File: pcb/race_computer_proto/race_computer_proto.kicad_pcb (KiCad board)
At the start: 4 copper layers, 200.7 x 125.7 mm, 17 parts, among them U1 Teensy4.0, U3 SN74LVC245APW

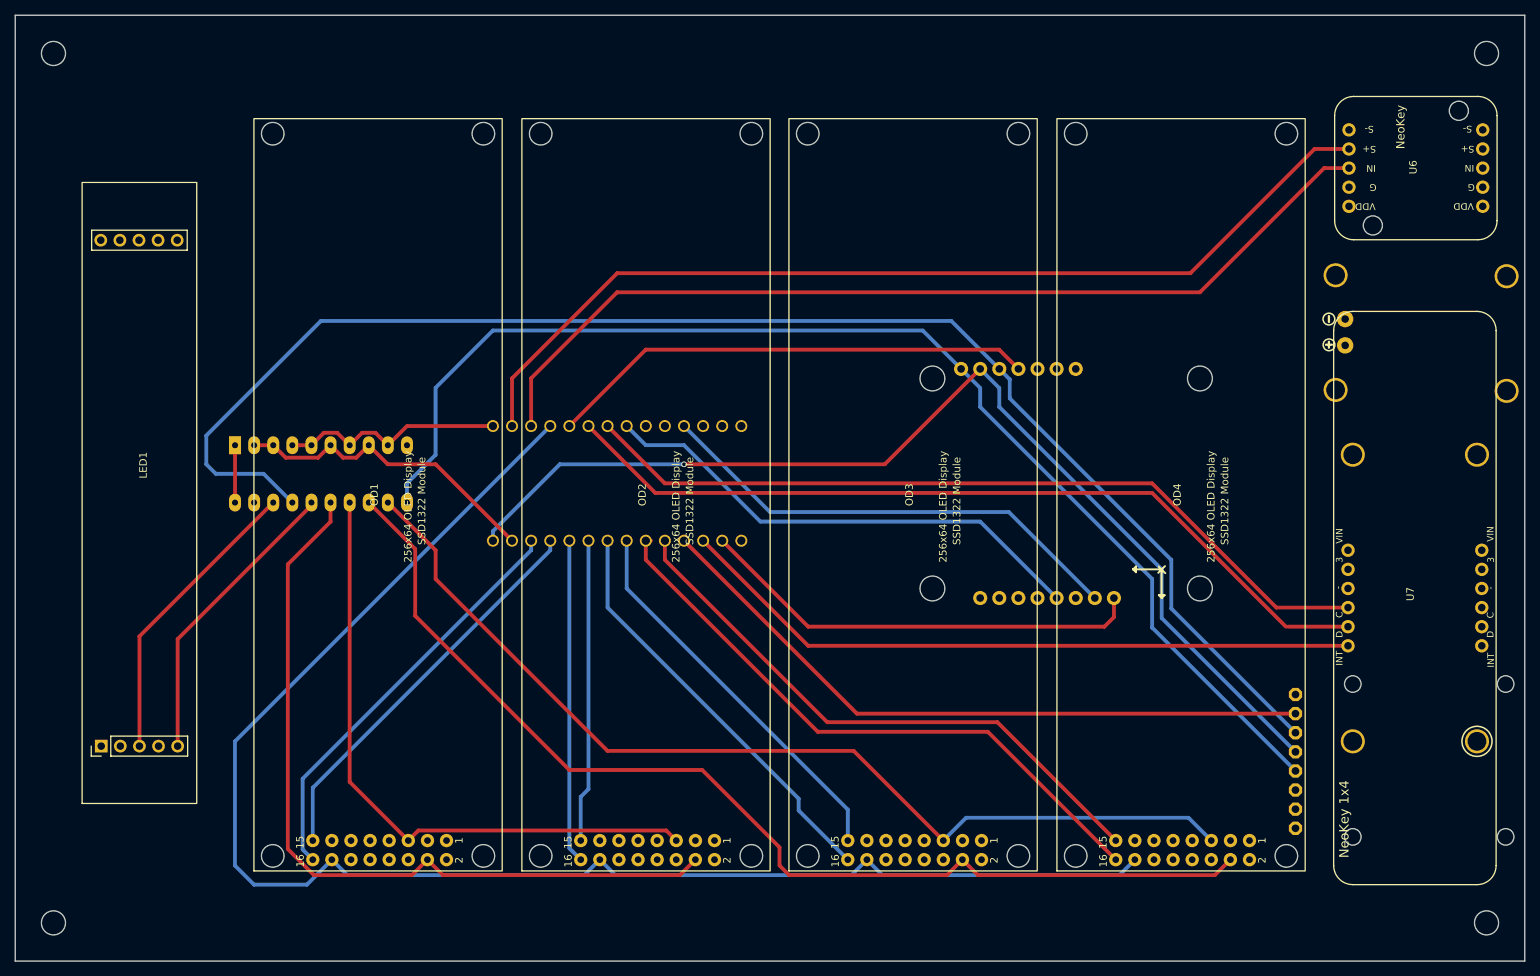
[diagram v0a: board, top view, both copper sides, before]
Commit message: Add missing chip select for LED display. Reorder OLED control pins so that GPS PPS signal is on Teensy pin 9. PPS must be on a pin that can be used as a timer input. Re-route PCB with above changes.
TODO:  Correct power board pinout (reversed).  Correct OLED connector pinour (mirrored).

Switch to callbacks for most GPS packet updates.
Displays now show: time delta, speed delta, distance remaining, distance traveled, speed, and average speed.
Enabled odometer and switched average speed calc to be based on the odometer.
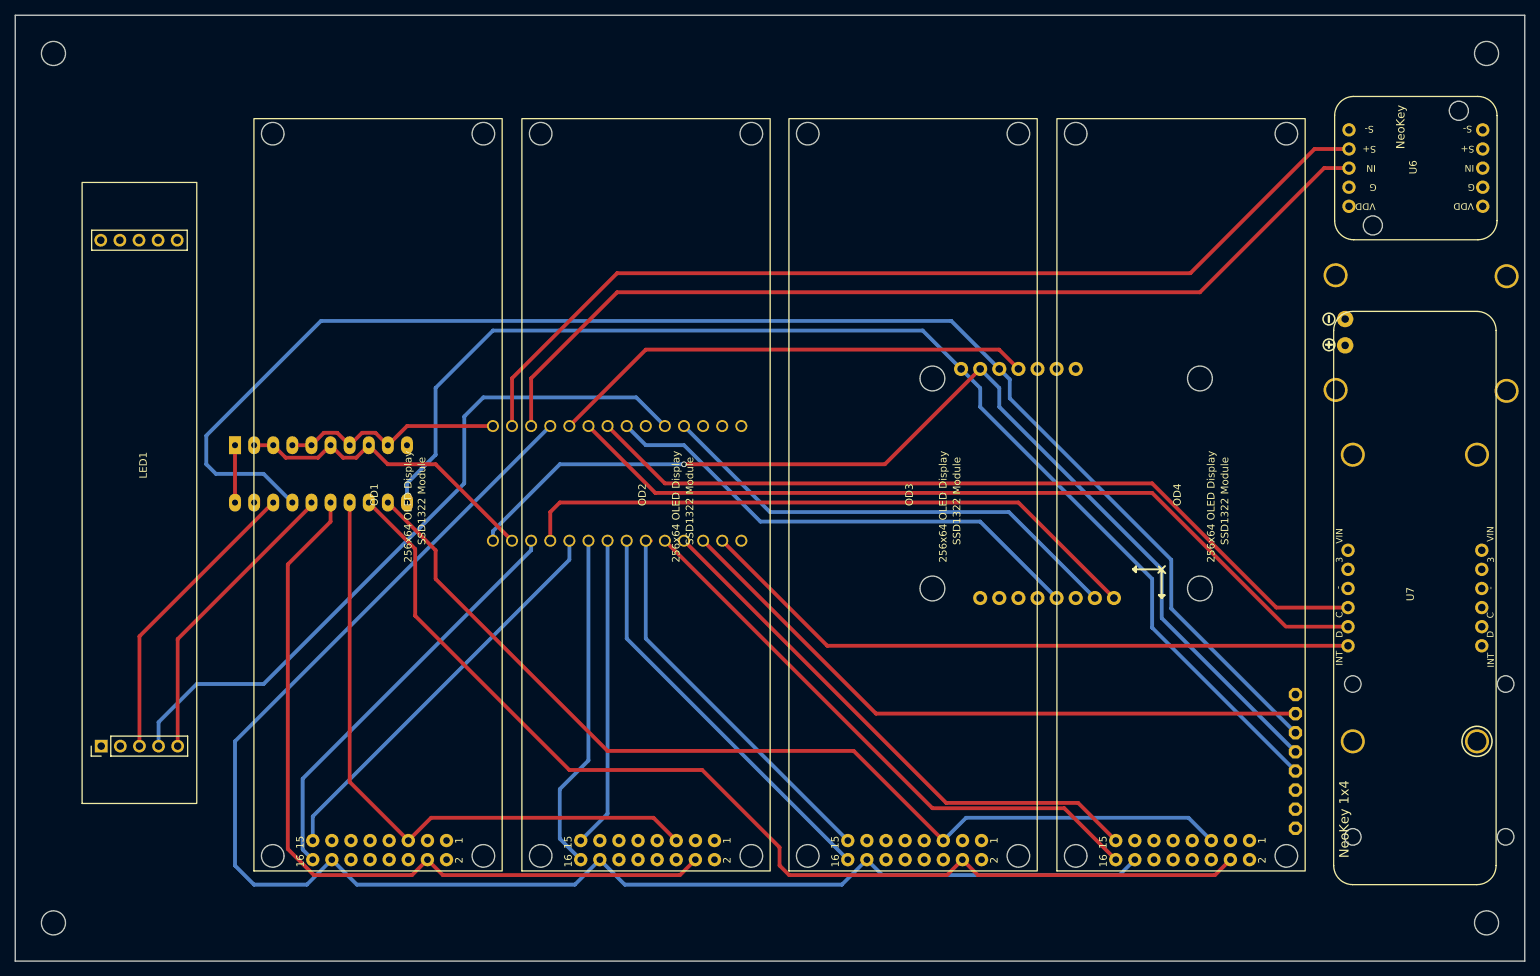
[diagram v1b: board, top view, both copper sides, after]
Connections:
- U1 pad 10: /DISP_BUS.CS1 -> /DISP_BUS.RESET0
- U1 pad 11: /DISP_BUS.RESET0 -> Net-(U1-9_OUT1C)
- U1 pad 2: Net-(U1-0_RX1_CRX2_CS1) -> /NEOKEY_INT
- U1 pad 29: unconnected-(U1-22_A8_CTX1-Pad29) -> /DISP_BUS.CS4
- U1 pad 3: /NEOKEY_INT -> /SDCARD_CS
- U1 pad 4: /SDCARD_CS -> /DISP_BUS.RESET3
- U1 pad 5: /DISP_BUS.RESET3 -> /DISP_BUS.CS3
- U1 pad 6: /DISP_BUS.CS3 -> /DISP_BUS.RESET2
- U1 pad 7: /DISP_BUS.RESET2 -> /DISP_BUS.CS2
- U1 pad 8: /DISP_BUS.CS2 -> /DISP_BUS.RESET1
- U1 pad 9: /DISP_BUS.RESET1 -> /DISP_BUS.CS1
- U2 pad 1: Net-(U1-0_RX1_CRX2_CS1) -> Net-(U1-9_OUT1C)
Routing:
- net /DISP_BUS.CS4: track 0.00 -> 95.2 mm
- net Net-(U1-9_OUT1C): track 0.00 -> 84.5 mm
- net Net-(U1-0_RX1_CRX2_CS1): track 59.9 -> 0.00 mm
- net /DISP_BUS.CS3: track 82.2 -> 77.5 mm
- net /DISP_BUS.RESET3: track 77.9 -> 73.9 mm
- net /SDCARD_CS: track 90.8 -> 88.3 mm
- net /NEOKEY_INT: track 91.5 -> 89.0 mm
- net /DISP_BUS.DC: track 202.9 -> 205.0 mm
- net /DISP_BUS.CS1: track 43.0 -> 45.1 mm
- net /DISP_BUS.MOSI0: track 84.9 -> 86.3 mm
- net /DISP_BUS.RESET1: track 40.3 -> 41.3 mm
- net /DISP_BUS.RESET0: track 52.9 -> 54.0 mm
- net /DISP_BUS.CS2: track 55.6 -> 54.6 mm

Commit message: Convert timer callback list to an object based event list to allow more flexible use. Add bitmaps for boot splash. Completed prototype case model. Corrected neokey breakout connections on schematic and PCB.  Removed only via from PCB.
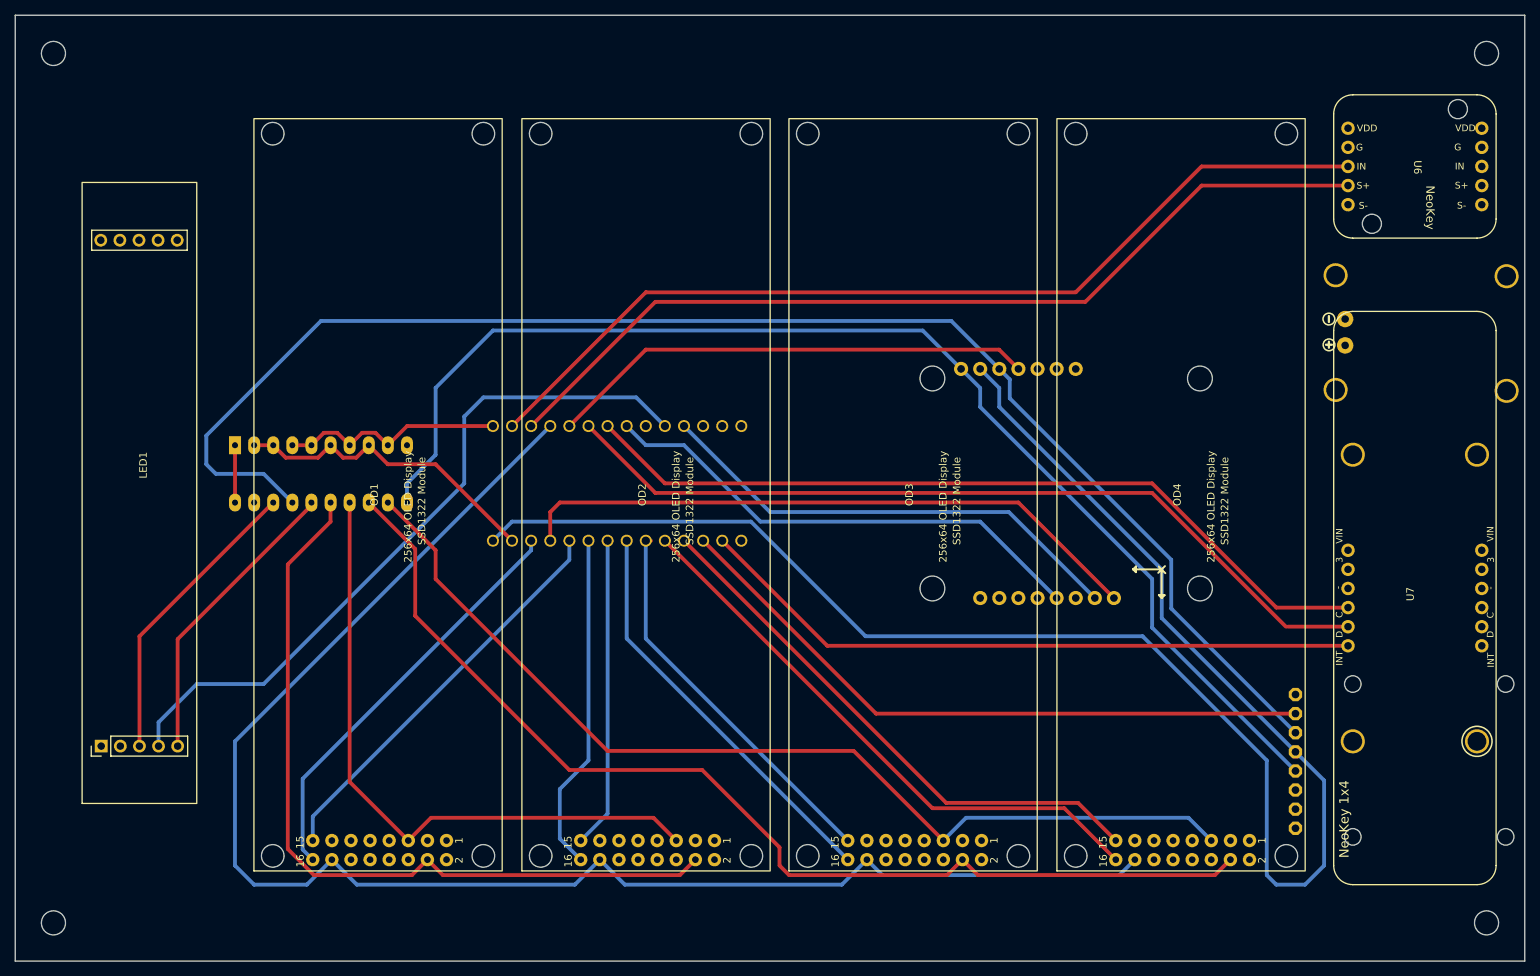
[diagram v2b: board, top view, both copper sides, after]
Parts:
- moved U6 0.42 mm to (235.4, 50.7), turned to -90 degrees
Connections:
- U6 pad 3: unconnected-(U6-NEO_IN-Pad3) -> Net-(U1-14_A0_TX3_SPDIF_OUT)
- U6 pad 4: unconnected-(U6-S+-Pad4) -> Net-(U1-15_A1_RX3_SPDIF_IN)
- U6 pad 7: Net-(U1-14_A0_TX3_SPDIF_OUT) -> unconnected-(U6-A-Pad7)
- U6 pad 8: Net-(U1-15_A1_RX3_SPDIF_IN) -> unconnected-(U6-NEO_OUT-Pad8)
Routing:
- net /MISO: track 143.2 -> 226.5 mm, vias 1 -> 0
- net Net-(U1-14_A0_TX3_SPDIF_OUT): track 130.2 -> 125.4 mm
- net Net-(U1-15_A1_RX3_SPDIF_IN): track 126.6 -> 121.8 mm

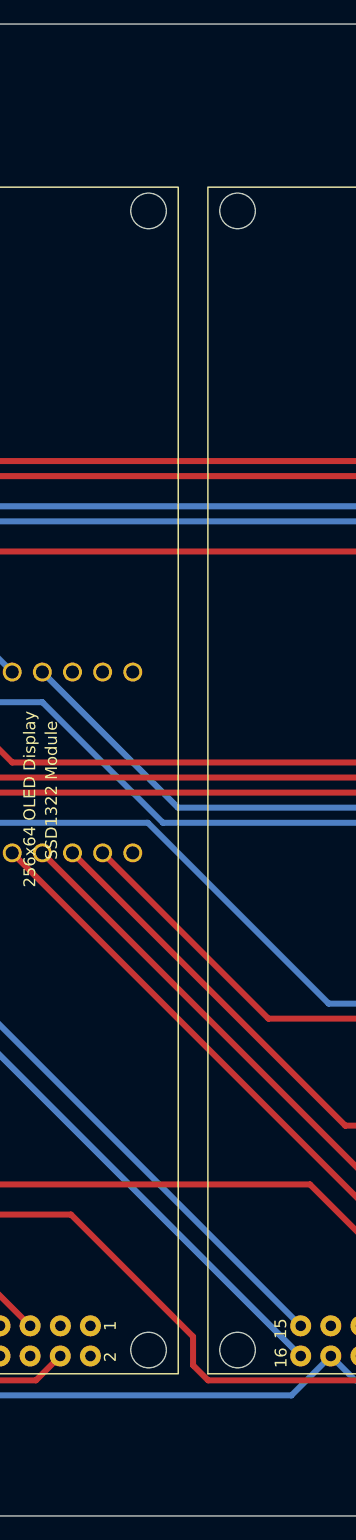
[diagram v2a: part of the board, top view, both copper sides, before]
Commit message: Correct an error on the case tongue and groove. Add a set of standoffs at the vertical midpoint of the case. Add matching holes in PCB for new standoffs. Fix formatting on OLED displays.
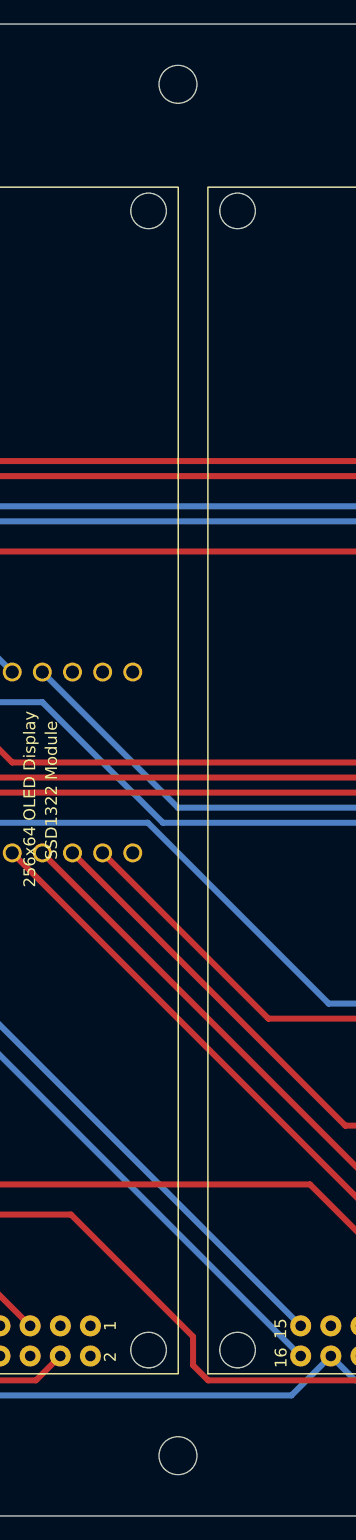
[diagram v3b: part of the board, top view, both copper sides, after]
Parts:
- added REF**: MountingHole_3.2mm_M3, MountingHole:MountingHole_3.2mm_M3, F.Cu at (149.9, 35.6)
- added REF**: MountingHole_3.2mm_M3, MountingHole:MountingHole_3.2mm_M3, F.Cu at (149.9, 151.1)
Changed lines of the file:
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@@
 		)
 	)
+	(footprint "MountingHole:MountingHole_3.2mm_M3"
+		(layer "F.Cu")
+		(at 149.86 35.56)
+		(descr "Mounting Hole 3.2mm, no annular, M3")
+		(tags "mounting hole 3.2mm no annular m3")
+		(property "Reference" "REF**"
+			(at 0 -4.2 0)
+			(layer "F.SilkS")
+			(hide yes)
+			(effects
+				(font
+					(size 1 1)
+					(thickness 0.15)
+				)
+			)
+		)
+		(property "Value" "MountingHole_3.2mm_M3"
+			(at 0 4.2 0)
+			(layer "F.Fab")
+			(effects
+				(font
+					(size 1 1)
+					(thickness 0.15)
+				)
+			)
+		)
+		(property "Footprint" "MountingHole:MountingHole_3.2mm_M3"
+			(at 0 0 0)
+			(unlocked yes)
+			(layer "F.Fab")
+			(hide yes)
+			(effects
+				(font
+					(size 1.27 1.27)
+					(thickness 0.15)
+				)
+			)
+		)
+		(property "Datasheet" ""
+			(at 0 0 0)
+			(unlocked yes)
+			(layer "F.Fab")
+			(hide yes)
+			(effects
+				(font
+					(size 1.27 1.27)
+					(thickness 0.15)
+				)
+			)
+		)
+		(property "Description" ""
+			(at 0 0 0)
+			(unlocked yes)
+			(layer "F.Fab")
+			(hide yes)
+			(effects
+				(font
+					(size 1.27 1.27)
+					(thickness 0.15)
+				)
+			)
+		)
+		(attr exclude_from_pos_files exclude_from_bom)
+		(fp_circle
+			(center 0 0)
+			(end 3.2 0)
+			(stroke
+				(width 0.15)
+				(type solid)
+			)
+			(fill none)
+			(layer "Cmts.User")
+		)
+		(fp_circle
+			(center 0 0)
+			(end 3.45 0)
+			(stroke
+				(width 0.05)
+				(type solid)
+			)
+			(fill none)
+			(layer "F.CrtYd")
+		)
+		(fp_text user "${REFERENCE}"
+			(at 0 0 0)
+			(layer "F.Fab")
+			(effects
+				(font
+					(size 1 1)
+					(thickness 0.15)
+				)
+			)
+		)
+		(pad "" np_thru_hole circle
+			(at 0 0)
+			(size 3.2 3.2)
+			(drill 3.2)
+			(layers "*.Cu" "*.Mask" "In3.Cu" "In4.Cu" "In5.Cu" "In6.Cu" "In7.Cu" "In8.Cu"
+				"In9.Cu" "In10.Cu" "In11.Cu" "In12.Cu" "In13.Cu" "In14.Cu" "In15.Cu"
+				"In16.Cu" "In17.Cu" "In18.Cu" "In19.Cu" "In20.Cu" "In21.Cu" "In22.Cu"
+				"In23.Cu" "In24.Cu" "In25.Cu" "In26.Cu" "In27.Cu" "In28.Cu" "In29.Cu"
+				"In30.Cu"
+			)
+		)
+	)
 	(footprint "race_computer:NeoKey1x4"
 		(layer "F.Cu")
@@
 			)
 		)
+	)
+	(footprint "MountingHole:MountingHole_3.2mm_M3"
+		(layer "F.Cu")
+		(at 149.86 151.13)
+		(descr "Mounting Hole 3.2mm, no annular, M3")
+		(tags "mounting hole 3.2mm no annular m3")
+		(property "Reference" "REF**"
+			(at 0 -4.2 0)
+			(layer "F.SilkS")
+			(hide yes)
+			(effects
+				(font
+					(size 1 1)
+					(thickness 0.15)
+				)
+			)
+		)
+		(property "Value" "MountingHole_3.2mm_M3"
+			(at 0 4.2 0)
+			(layer "F.Fab")
+			(effects
+				(font
+					(size 1 1)
+					(thickness 0.15)
+				)
+			)
+		)
+		(property "Footprint" "MountingHole:MountingHole_3.2mm_M3"
+			(at 0 0 0)
+			(unlocked yes)
+			(layer "F.Fab")
+			(hide yes)
+			(effects
+				(font
+					(size 1.27 1.27)
+					(thickness 0.15)
+				)
+			)
+		)
+		(property "Datasheet" ""
+			(at 0 0 0)
+			(unlocked yes)
+			(layer "F.Fab")
+			(hide yes)
+			(effects
+				(font
+					(size 1.27 1.27)
+					(thickness 0.15)
+				)
+			)
+		)
+		(property "Description" ""
+			(at 0 0 0)
+			(unlocked yes)
+			(layer "F.Fab")
+			(hide yes)
+			(effects
+				(font
+					(size 1.27 1.27)
+					(thickness 0.15)
+				)
+			)
+		)
+		(attr exclude_from_pos_files exclude_from_bom)
+		(fp_circle
+			(center 0 0)
+			(end 3.2 0)
+			(stroke
+				(width 0.15)
+				(type solid)
+			)
+			(fill none)
+			(layer "Cmts.User")
+		)
+		(fp_circle
+			(center 0 0)
+			(end 3.45 0)
+			(stroke
+				(width 0.05)
+				(type solid)
+			)
+			(fill none)
+			(layer "F.CrtYd")
+		)
+		(fp_text user "${REFERENCE}"
+			(at 0 0 0)
+			(layer "F.Fab")
+			(effects
+				(font
+					(size 1 1)
+					(thickness 0.15)
+				)
+			)
+		)
+		(pad "" np_thru_hole circle
+			(at 0 0)
+			(size 3.2 3.2)
+			(drill 3.2)
+			(layers "*.Cu" "*.Mask" "In3.Cu" "In4.Cu" "In5.Cu" "In6.Cu" "In7.Cu" "In8.Cu"
+				"In9.Cu" "In10.Cu" "In11.Cu" "In12.Cu" "In13.Cu" "In14.Cu" "In15.Cu"
+				"In16.Cu" "In17.Cu" "In18.Cu" "In19.Cu" "In20.Cu" "In21.Cu" "In22.Cu"
+				"In23.Cu" "In24.Cu" "In25.Cu" "In26.Cu" "In27.Cu" "In28.Cu" "In29.Cu"
+				"In30.Cu"
+			)
+		)
